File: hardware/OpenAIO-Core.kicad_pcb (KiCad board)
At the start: 6 copper layers, 23 x 20.1 mm, 87 parts, among them J23 5V, J26 5V, J30 5V, J34 5V, J35 5V, J37 5V, J38 5V, J39 5V, J40 5V, J41 5V, J42 5V, J43 5V, J44 5V, J45 5V, J48 5V, J49 5V, J50 5V, J51 5V, J52 5V, J53 5V, J54 5V, J55 5V, J91 Core_LGA, Q1 AP1606, Q2 AP1606, U1 TS2306A 240GF MSM 9_C2976675, U10 COS8051SOT, U11 TLV7031DPWR, U2 RP2354A, U6 LP5912-1.8DRVR, U8 BMI270, U9 SN74LVC1G3157DTBR, X1 XTM25012000JT00351001

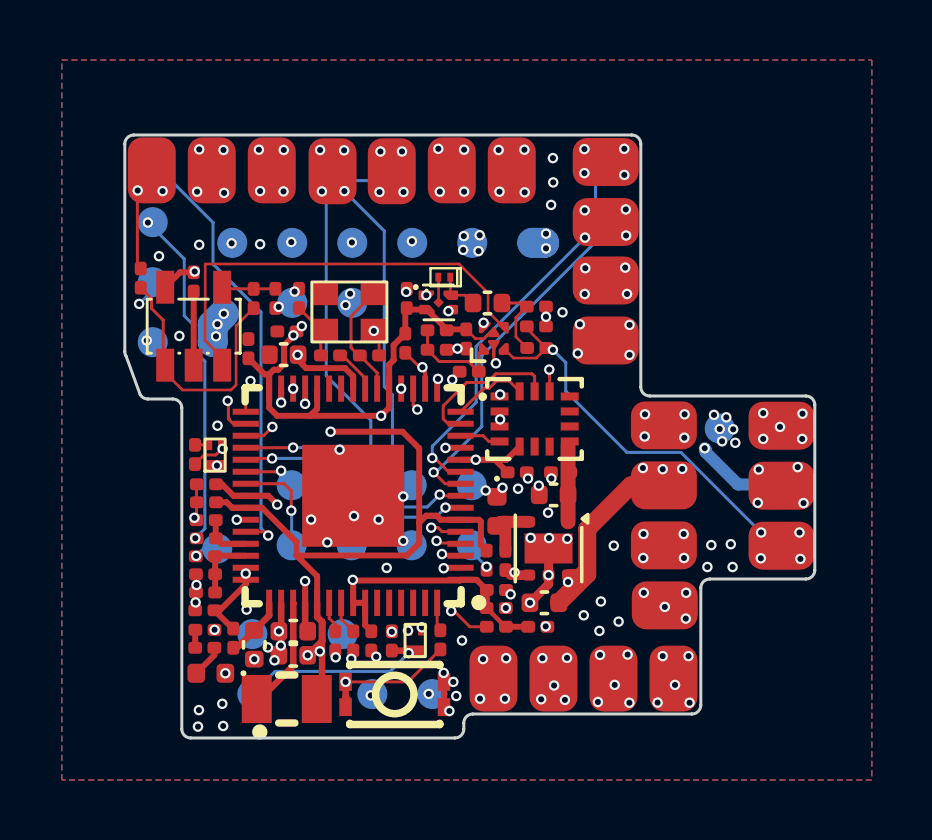
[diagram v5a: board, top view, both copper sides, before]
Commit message: OpenAIO: LGA +4v5 pin added
Co-Authored-By: Claude Fable 5 <noreply@anthropic.com>
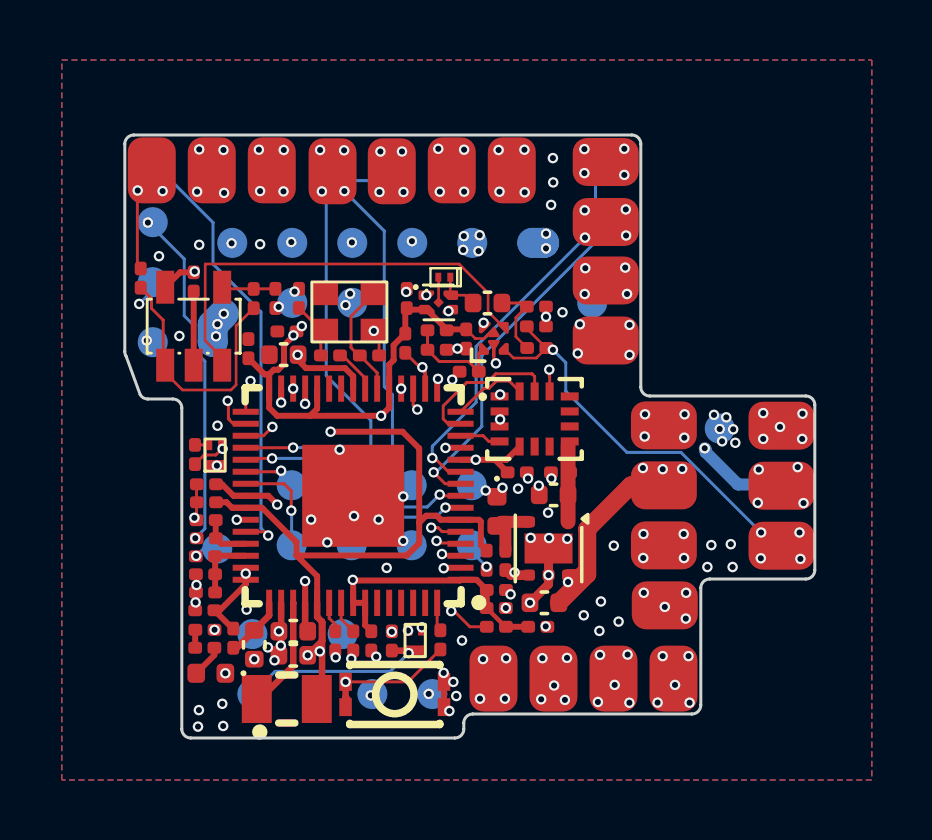
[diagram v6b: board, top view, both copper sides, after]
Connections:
- J91 pad 12: USB_D- -> +4v5
- J91 pad 13: +5V -> USB_D-
- J91 pad 14: GND -> +5V
- J91 pad 16: MOTOR2 -> GND
- J91 pad 17: MOTOR4 -> MOTOR2
- J91 pad 18: GND -> MOTOR4
- J91 pad 20: BUZZER- -> GND
- J91 pad 21: MOTOR1 -> BUZZER-
- J91 pad 22: MOTOR3 -> MOTOR1
- J91 pad 23: GND -> MOTOR3
- J91 pad 25: +BATT -> GND
- J91 pad 26: GND -> +BATT
- J91 pad 29: UART0_TX -> GND
- J91 pad 30: UART0_RX -> UART0_TX
- J91 pad 31: LED_STRIP -> UART0_RX
- J91 pad 32: UART1_RX -> LED_STRIP
- J91 pad 33: UART1_TX -> UART1_RX
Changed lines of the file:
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@@
 		)
 		(pad "12" smd circle
+			(at -4.2 4.18 180)
+			(size 1 1)
+			(layers "B.Cu" "B.Mask")
+			(net "+4v5")
+		)
+		(pad "13" smd circle
 			(at 10.45 2.87 180)
 			(size 1 1)
@@
 			(net "USB_D-")
 		)
-		(pad "13" smd circle
+		(pad "14" smd circle
 			(at 8.45 2.88 180)
 			(size 1 1)
@@
 			(net "+5V")
 		)
-		(pad "14" smd circle
+		(pad "15" smd circle
 			(at -8.45 -0.01 180)
 			(size 1 1)
@@
 			(net "GND")
 		)
-		(pad "15" smd circle
+		(pad "16" smd circle
 			(at -10.45 -0.01 180)
 			(size 1 1)
@@
 			(net "GND")
 		)
-		(pad "16" smd circle
+		(pad "17" smd circle
 			(at 5.82 -1.9 180)
 			(size 1 1)
@@
 			(net "MOTOR2")
 		)
-		(pad "17" smd circle
+		(pad "18" smd circle
 			(at 3.82 -1.9 180)
 			(size 1 1)
@@
 			(net "MOTOR4")
 		)
-		(pad "18" smd circle
+		(pad "19" smd circle
 			(at 1.82 -1.9 180)
 			(size 1 1)
@@
 			(net "GND")
 		)
-		(pad "19" smd circle
+		(pad "20" smd circle
 			(at -0.18 -1.9 180)
 			(size 1 1)
@@
 			(net "GND")
 		)
-		(pad "20" smd circle
+		(pad "21" smd circle
 			(at -10.45 -2.01 180)
 			(size 1 1)
@@
 			(net "BUZZER-")
 		)
-		(pad "21" smd circle
+		(pad "22" smd circle
 			(at 5.82 -3.9 180)
 			(size 1 1)
@@
 			(net "MOTOR1")
 		)
-		(pad "22" smd circle
+		(pad "23" smd circle
 			(at 3.82 -3.9 180)
 			(size 1 1)
@@
 			(net "MOTOR3")
 		)
-		(pad "23" smd circle
+		(pad "24" smd circle
 			(at 1.82 -3.9 180)
 			(size 1 1)
@@
 			(net "GND")
 		)
-		(pad "24" smd circle
+		(pad "25" smd circle
 			(at -0.18 -3.9 180)
 			(size 1 1)
@@
 			(net "GND")
 		)
-		(pad "25" smd circle
+		(pad "26" smd circle
 			(at 8.3 -4.01 180)
 			(size 1 1)
@@
 			(net "+BATT")
 		)
-		(pad "26" smd circle
+		(pad "27" smd circle
 			(at 7.13 -6.86 180)
 			(size 1 1)
@@
 			(net "GND")
 		)
-		(pad "27" smd circle
+		(pad "28" smd circle
 			(at 4.12 -6.86 180)
 			(size 1 1)
@@
 			(net "GND")
 		)
-		(pad "28" smd circle
+		(pad "29" smd circle
 			(at -2.97 -8.56 180)
 			(size 1 1)
@@
 			(net "GND")
 		)
-		(pad "29" smd circle
+		(pad "30" smd circle
 			(at -4.97 -8.56 180)
 			(size 1 1)
@@
 			(net "UART0_TX")
 		)
-		(pad "30" smd circle
+		(pad "31" smd circle
 			(at -6.97 -8.56 180)
 			(size 1 1)
@@
 			(net "UART0_RX")
 		)
-		(pad "31" smd circle
+		(pad "32" smd circle
 			(at 7.13 -8.86 180)
 			(size 1 1)
@@
 			(net "LED_STRIP")
 		)
-		(pad "32" smd circle
+		(pad "33" smd circle
 			(at 3.13 -8.86 180)
 			(size 1 1)
@@
 			(net "UART1_RX")
 		)
-		(pad "33" smd circle
+		(pad "34" smd circle
 			(at 1.13 -8.86 180)
 			(size 1 1)

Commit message: OpenAIO: Base and Core routing progress; README states the two-board design as drawn
Co-Authored-By: Claude Fable 5 <noreply@anthropic.com>
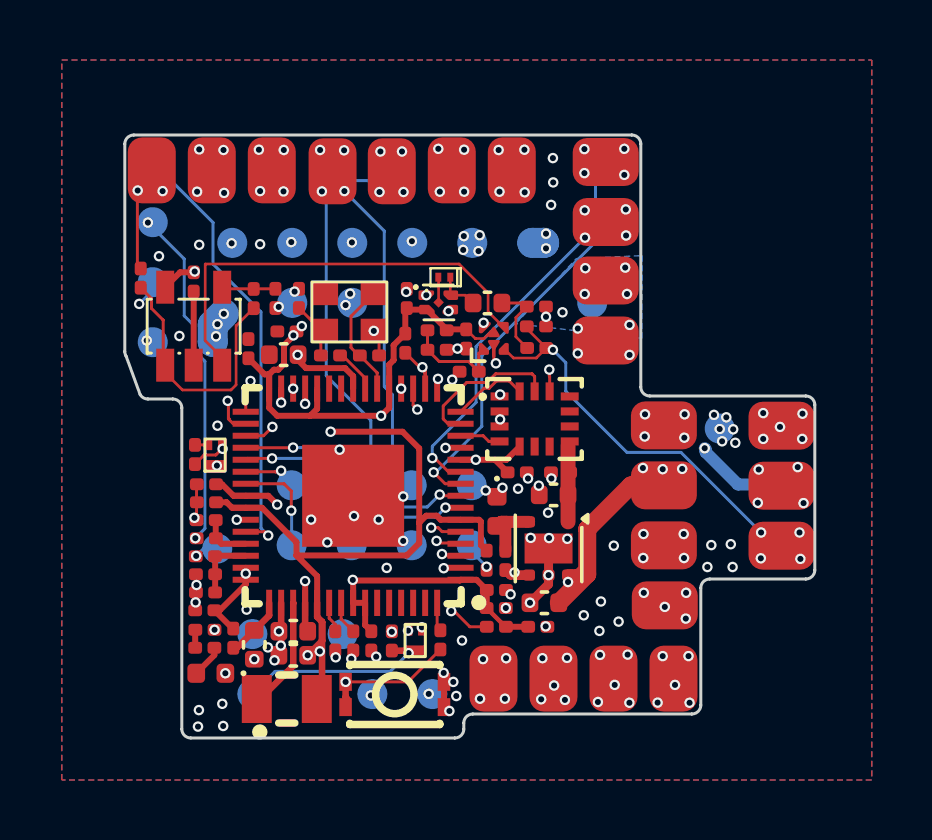
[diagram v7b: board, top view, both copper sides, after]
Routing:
- added copper zone on B.Cu, net +4v5
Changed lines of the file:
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@@
 	)
 	(via
-		(at 118.27 49.81)
+		(at 118.2 49.95)
 		(size 0.35)
 		(drill 0.2)
@@
 			)
 		)
+	)
+	(zone
+		(net "+4v5")
+		(layer "B.Cu")
+		(hatch edge 0.5)
+		(priority 4)
+		(connect_pads yes
+			(clearance 0.12)
+		)
+		(min_thickness 0.25)
+		(fill yes
+			(thermal_gap 0.5)
+			(thermal_bridge_width 0.5)
+			(island_removal_mode 0)
+		)
+		(polygon
+			(pts
+				(xy 118.15 47.62) (xy 120.35 47.52) (xy 120.34 50.28) (xy 116.13 49.79)
+			)
+		)

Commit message: Base fully routed (recovered from KiCad local history, 2026-08-22)
The finished Base route was never committed: the last Base commit (ce0aa59)
had 57 unconnected. Recovered from hardware/.history snapshot 55d048e
(last save 2026-08-22 15:03), on top of ce0aa59.

DRC (kicad-cli 10):
- Base: 0 unconnected, 0 shorts, 6 errors (3 x U23 own pad-to-pad
  clearance, USB1 NPTH: 1 clearance + 2 annular width), 111 warnings
- Core: 0 unconnected, 0 errors

Co-Authored-By: Claude Opus 5.5 <noreply@anthropic.com>
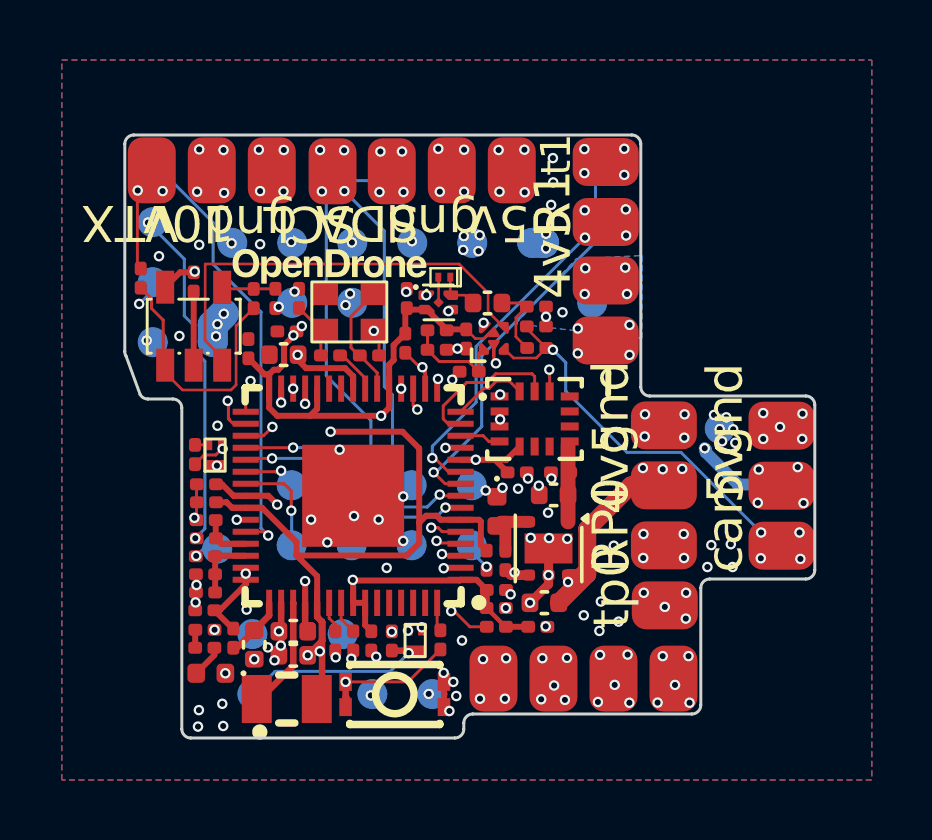
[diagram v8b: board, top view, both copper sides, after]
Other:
- board text added: "10v"
- board text added: "4v5"
- board text added: "5v"
- board text added: "R1"
- board text added: "RP0"
- board text added: "SCL"
- board text added: "SDA"
- board text added: "VTX"
- board text added: "cam"
- board text added: "gnd"
- board text added: "t1"
- board text added: "tp0"
